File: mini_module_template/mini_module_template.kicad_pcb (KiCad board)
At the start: 4 copper layers, 100 x 50 mm, 129 parts, among them IC1 TJA1044GTK_3Z, J1 SWD, J4 USB_C_Receptacle_USB2.0, Q1 S9013, SW2 NRST, SW4 SW_DIP_x01, U1 STM32F303CBTx, U2 FM24CL16B, U3 STM32F103CB, U4 AZ1117-3.3, U5 TPS563200, U6 IP4220CZ6, U7 SL2.1A, Y1 8MHz, Y2 8MHz

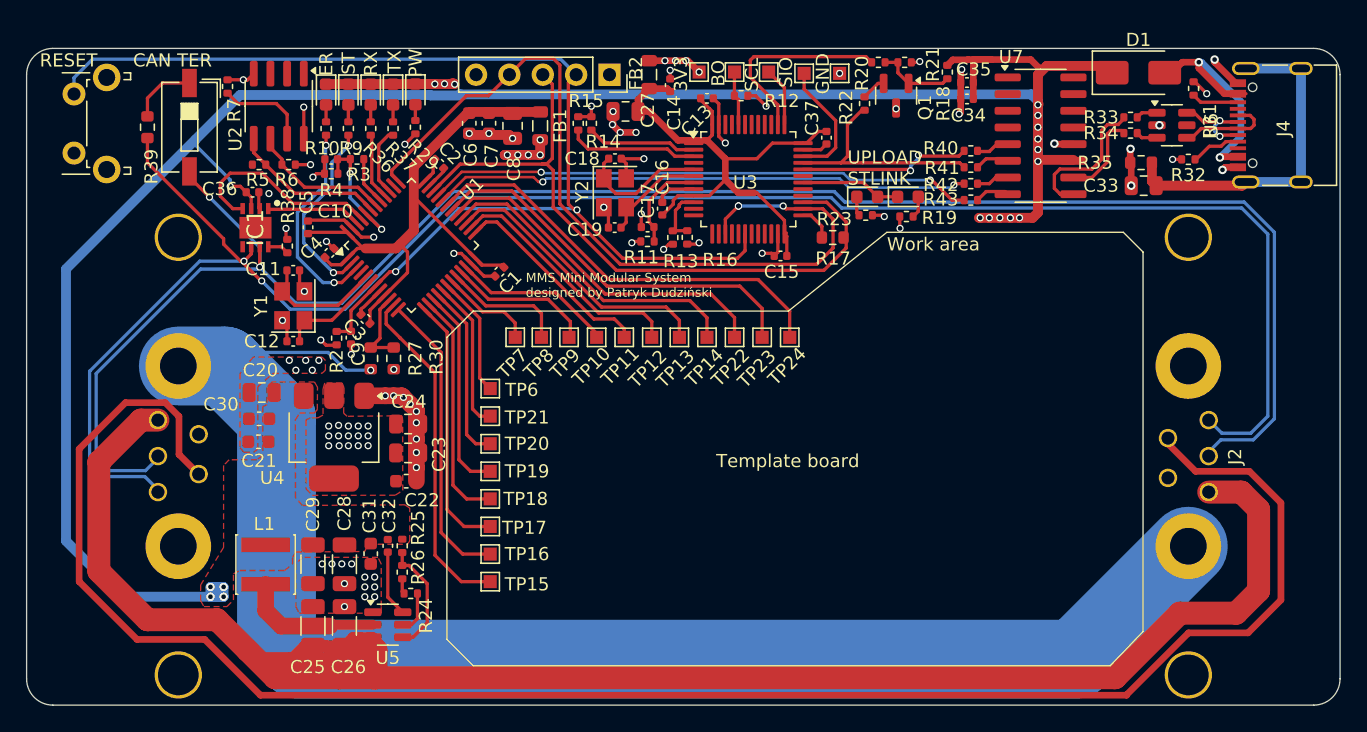
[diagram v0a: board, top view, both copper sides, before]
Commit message: addded crystal to usb hub. added connection tabs to stm+stlink
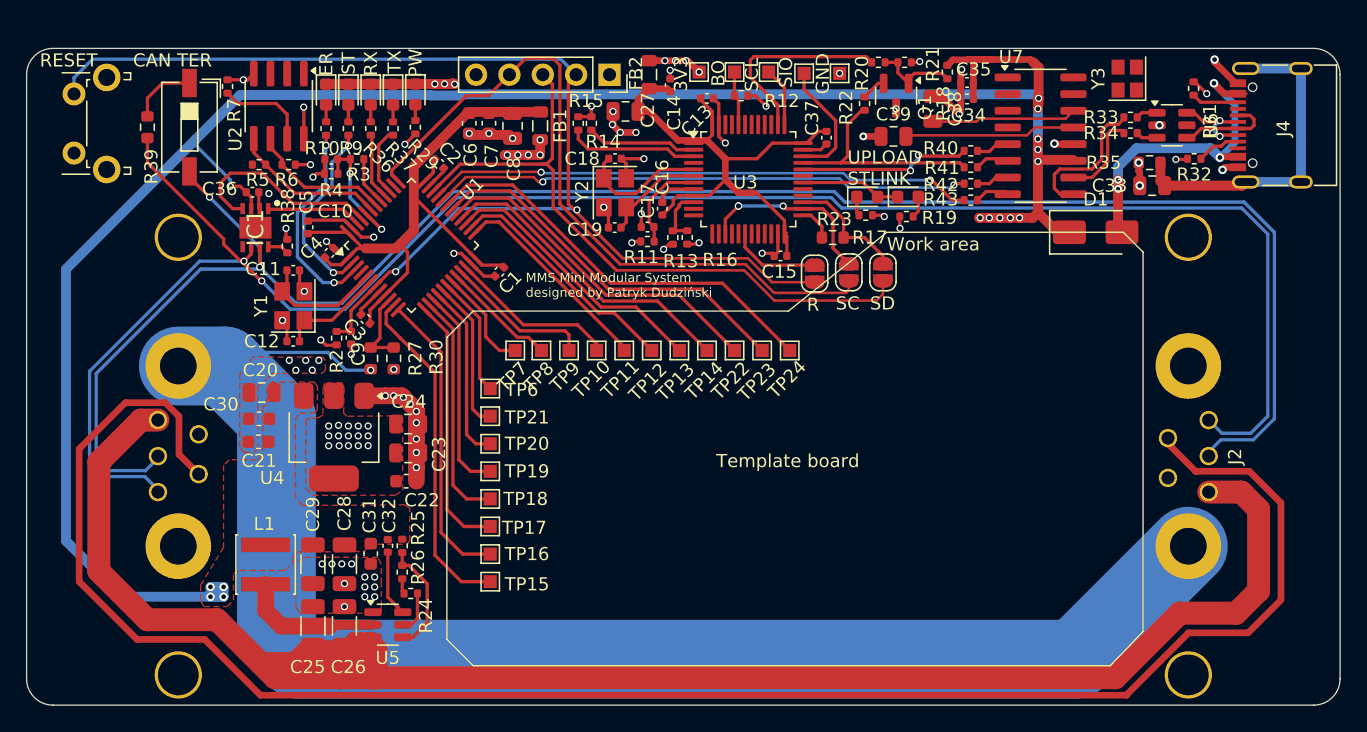
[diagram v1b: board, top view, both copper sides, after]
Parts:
- added C38: 10u, Capacitor_SMD:C_0805_2012Metric, F.Cu at (149.0, 64.6)
- added C39: 10u, Capacitor_SMD:C_0805_2012Metric, F.Cu at (146.0, 66.7)
- added JP1: SolderJumper_2_Bridged, Jumper:SolderJumper-2_P1.3mm_Open_RoundedPad1.0x1.5mm, F.Cu at (142.6, 77.0)
- added JP2: SolderJumper_2_Bridged, Jumper:SolderJumper-2_P1.3mm_Open_RoundedPad1.0x1.5mm, F.Cu at (145.2, 77.0)
- added JP3: SolderJumper_2_Bridged, Jumper:SolderJumper-2_P1.3mm_Open_RoundedPad1.0x1.5mm, F.Cu at (140.0, 77.2)
- added Y3: 12Mhz, Crystal:Crystal_SMD_2520-4Pin_2.5x2.0mm, F.Cu at (163.8, 62.3)
- moved D1 12.6 mm to (161.4, 74.0)
- moved TP10 1.00 mm to (123.4, 83.0)
- moved TP11 1.00 mm to (125.5, 83.0)
- moved TP12 1.00 mm to (127.6, 83.0)
- moved TP13 1.00 mm to (129.7, 83.0)
- moved TP14 1.00 mm to (131.8, 83.0)
- moved TP22 1.00 mm to (133.9, 83.0)
- moved TP23 1.00 mm to (136.0, 83.0)
- moved TP24 1.00 mm to (138.1, 83.0)
- moved TP7 1.00 mm to (117.2, 83.0)
- moved TP8 1.00 mm to (119.2, 83.0)
- moved TP9 1.00 mm to (121.3, 83.0)
- moved R35 0.65 mm to (165.5, 68.7)
- moved C33 0.65 mm to (165.7, 70.5)
- moved R32 0.45 mm to (168.9, 68.4)
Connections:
- R17 pad 2: /MCU/SWDIO -> /STLINK/SWDIO
- U3 pad 15: /MCU/SWCLK -> /STLINK/SWCLK
- U3 pad 18: /MCU/NRST -> /STLINK/NRST
- U3 pad 26: /MCU/SWCLK -> /STLINK/SWCLK
- U3 pad 27: /MCU/SWDIO -> /STLINK/SWDIO
- U7 pad 13: unconnected-(U7-VDD33-Pad13) -> Net-(U7-VDD33)
- U7 pad 14: unconnected-(U7-VDD18-Pad14) -> Net-(U7-VDD18)
- U7 pad 15: unconnected-(U7-XOUT-Pad15) -> Net-(U7-XOUT)
- U7 pad 16: unconnected-(U7-XIN-Pad16) -> Net-(U7-XIN)
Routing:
- net /STLINK/SWCLK: track 0.00 -> 14.1 mm, vias 0 -> 3
- net Net-(U7-VDD33): track 0.00 -> 13.0 mm
- net Net-(U7-VDD18): track 0.00 -> 11.1 mm
- net /MCU/SWCLK: track 64.4 -> 54.4 mm, vias 3 -> 0
- net /STLINK/SWDIO: track 0.00 -> 9.20 mm
- net Net-(D1-A): track 18.3 -> 25.4 mm, vias 2 -> 4
- net /STLINK/NRST: track 0.00 -> 6.88 mm
- net /MCU/NRST: track 90.5 -> 95.0 mm
- net +5V: track 168.3 -> 164.7 mm, vias 16 -> 15
- net GND: track 92.6 -> 95.7 mm, vias 69 -> 70
- net /MCU/SWDIO: track 52.2 -> 50.5 mm
- net PA9: track 30.1 -> 29.2 mm
- net PA10: track 32.6 -> 31.9 mm
- net PB1: track 7.32 -> 8.06 mm
- net Net-(J4-SHIELD): track 25.9 -> 25.2 mm
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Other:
- board text added: "R"
- board text added: "SC"
- board text added: "SD"

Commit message: ?
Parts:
- removed Y3: 12Mhz, Crystal:Crystal_SMD_2520-4Pin_2.5x2.0mm
- added Y4: 12Mhz, Crystal:Crystal_SMD_3225-4Pin_3.2x2.5mm, F.Cu at (163.2, 62.4)
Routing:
- net Net-(U7-XOUT): track 0.00 -> 5.40 mm
- net Net-(U7-XIN): track 0.00 -> 3.03 mm
- net GND: vias 70 -> 72
